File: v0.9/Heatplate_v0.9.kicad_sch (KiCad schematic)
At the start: 43 parts, among them J1 Barrel_Jack_Switch, Q1 WSP4409A, Q2 IRLR8726TRPBF, Q3 SS8050, U1 ATMEGA4809-AFR, U2 AMS1117-5.0

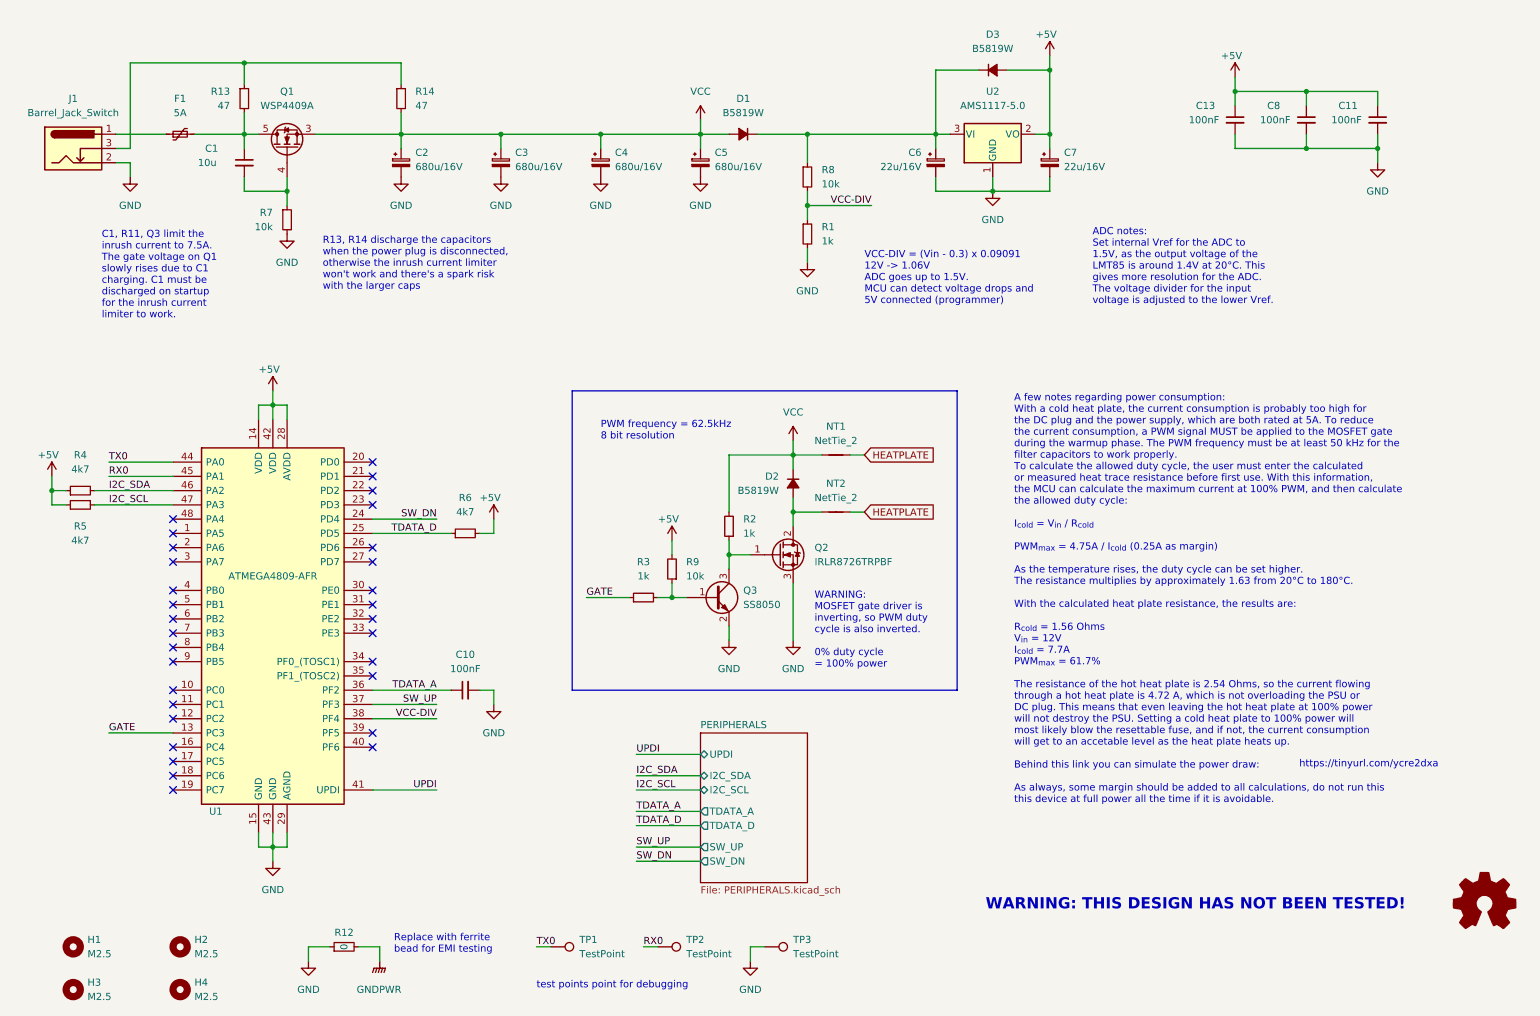
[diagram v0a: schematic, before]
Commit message: Add files via upload
status LEDs added
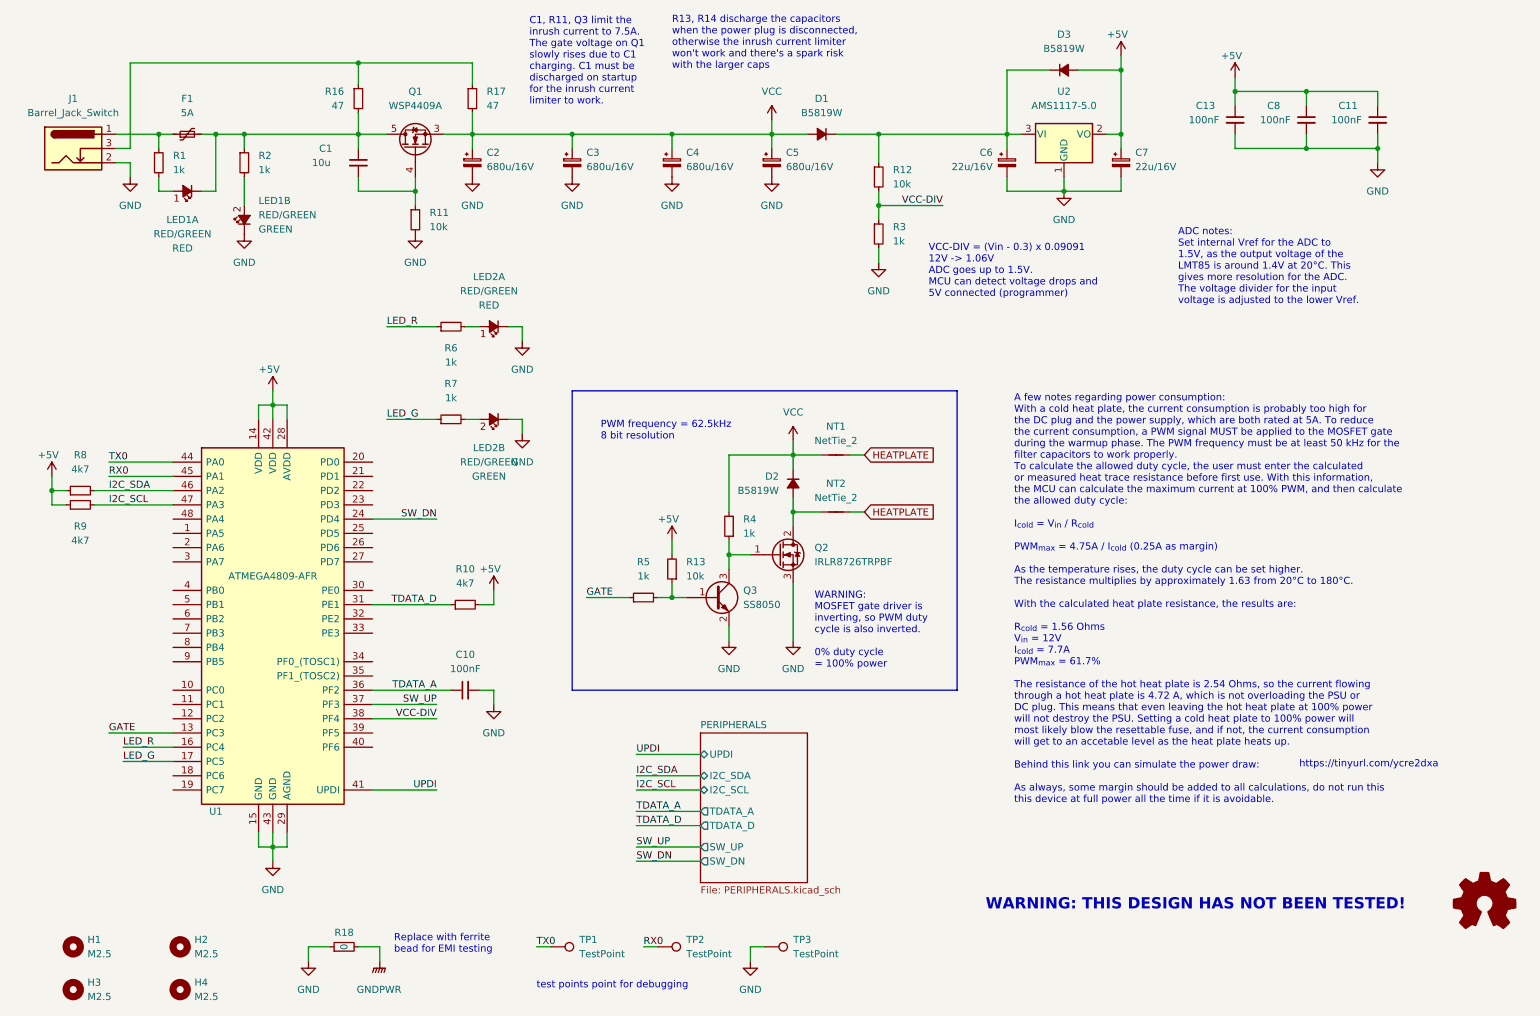
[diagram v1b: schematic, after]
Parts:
- added LED1, LED2: RED/GREEN, LED_SMD:LED_Avago_PLCC4_3.2x2.8mm_CW, symbol User:LED_Dual_AKAK_Split_Small_Filled
- added R1, R2, R6, R7: 1k, Resistor_SMD:R_0805_2012Metric, symbol Device:R_Small
- C1: LCSC Part Number C2922480 -> C440198
- C10, C11, C13, C8: LCSC Part Number C1711 -> C49678
- R18: renamed from R12; LCSC Part Number C25275 -> C17477
- renumbered R6 to R10, R7 to R11, R8 to R12, R9 to R13, R13 to R16, R14 to R17, R1 to R3, R2 to R4, R3 to R5, R4 to R8, R5 to R9
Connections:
- net GND: now also LED1.4 (K2), LED2.2 (K1), LED2.4 (K2)
- net TDATA_D: now also U1.31 (PE1); no longer U1.25 (PD5)
- net at C1.1, F1.2, Q1.5 (D)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: now also LED1.2 (K1), R2.1
- net at F1.1, J1.1: now also R1.1
- net LED_R: now reaches U1.16 (PC4)
- net LED_R: now also R6.1
- net LED_G: now reaches U1.17 (PC5)
- net LED_G: now also R7.1
- new net: LED2.3 (A2), R7.2
- new net: LED1.3 (A2), R2.2
- new net: LED2.1 (A1), R6.2
- new net: LED1.1 (A1), R1.2
- no-connect marks 31 -> 0
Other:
- moved on the sheet: C1, C2, C3, C4, C5, C6, C7, D1, D3, F1, Q1, R10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

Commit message: error in LED2 footprint fixed
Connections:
- net LED_G: now also R6.1, U1.16 (PC4); no longer R7.1, U1.17 (PC5)
- net LED_R: now also R7.1, U1.17 (PC5); no longer R6.1, U1.16 (PC4)
- net at LED2.3 (A2): now also R6.2; no longer R7.2
- net at LED2.1 (A1): now also R7.2; no longer R6.2
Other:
- moved on the sheet: LED2A, LED2B
